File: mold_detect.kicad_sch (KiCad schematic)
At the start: 39 parts, among them J1 USB_C_Receptacle_USB2.0_14P, U1 SHT30-DIS, U2 TPL5010, U3 FT230XS, U4 W25Q128JVS, U5 ATmega328P-P, Y1 4MHz

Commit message: tpl5010 works!
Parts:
- added J2: ISP, Connector_IDC:IDC-Header_2x03_P2.54mm_Vertical, symbol Connector_Generic:Conn_02x03_Odd_Even
- added R11, R12: 100R, Resistor_SMD:R_0603_1608Metric_Pad0.98x0.95mm_HandSolder, symbol Device:R
- added Red2, Red3: LED, LED_THT:LED_D3.0mm, symbol Device:LED
- added SW2: usb_enable, symbol Switch:SW_DIP_x01
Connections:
- net +3V0: now also J2.2 (Pin_2)
- net CIPO: now also J2.1 (Pin_1)
- net COPI: now also J2.4 (Pin_4)
- net DONE: now also U5.6 (PD4); no longer U5.5 (PD3)
- net GND: now also R1.1, R2.1, J2.6 (Pin_6), R11.1, R12.1, SW2.1; no longer R1.2, R2.2, U3.13 (GND), U3.5 (GND)
- net HUM_LED: now also Blue1.2 (A); no longer Red1.2 (A)
- net RST: now also J2.5 (Pin_5)
- net SCK: now also J2.3 (Pin_3)
- net TEMP_LED: now also Red2.2 (A); no longer Blue1.2 (A)
- net WAKE_INTR: now also U5.5 (PD3); no longer U5.4 (PD2)
- net ERROR_LED: now reaches U5.13 (PD7)
- net ERROR_LED: now also Red1.2 (A)
- net USB_ENABLE_INTR: now reaches U5.23 (PC0)
- net USB_ENABLE_INTR: now also U3.13 (GND), U3.5 (GND), SW2.2
- net at Red1.1 (K): now also R11.2; no longer R1.1
- net at Blue1.1 (K): now also R2.2; no longer R2.1
- new net: R1.2, Red2.1 (K)
- new net: R12.2, Red3.1 (K)
- new net GENERAL_LED: Red3.2 (A), U5.4 (PD2)
- no-connect marks 18 -> 15
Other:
- note added: "ISP Port"
- note added: "The *two* 5k1 resistors at the C1 and C2 pins configure the USB C port for USB 2.0 operation. These aren't used when using a USB-A to USB-C cable. The USB Bus Powered Configuration is used (data sheet p. 18). The diode is needed to prevent the initial 3V3 laying on the USB-C port's VBUS when using a USB-C to USB-C cable. Without this the USB-C host won't enable USB 2.0 at 5V operation. The enable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"
- note added: "USB-C Port"
- note added: "Using 4MHz crystal and the internal 8div a clock speed of 0MHz5 is achieved. The internal crystal isn't accurate enough for UART. All unused pins will have an active internal pull up resistor and are configured as inputs to prevent a floating value. Using an external pull up could reduce power consumption. The internal pull-up on USB_ENABLE_INTR (PC0) is enabled. The one on WAKE_INTR (PD3) is dis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"
- note removed: "Port"
- note removed: "The *two* 5k1 resistors at the C1 and C2 pins configure the USB C port for USB 2.0 operation. These aren't used when using a USB-A to USB-C cable. The USB Bus Powered Configuration is used (data sheet p. 18). The diode is needed to prevent the initial 3V3 laying on the USB-C port's VBUS when using a USB-C to USB-C cable. Without this the USB-C host won't enable USB 2.0 at 5V operation."
- note removed: "Using 4MHz crystal and the internal 8div a clock speed of 0MHz5 is achieved. The internal crystal isn't accurate enough for UART. All unused pins will have an active internal pull up resistor and are configured as inputs to prevent a floating value. Using an external pull up could reduce power consumption."
- note removed: "high hum"
- note removed: "low temp"
- moved on the sheet: BT1, Blue1, C1, C10, C11, C2, C3, C4, C5, C6, C7, C8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

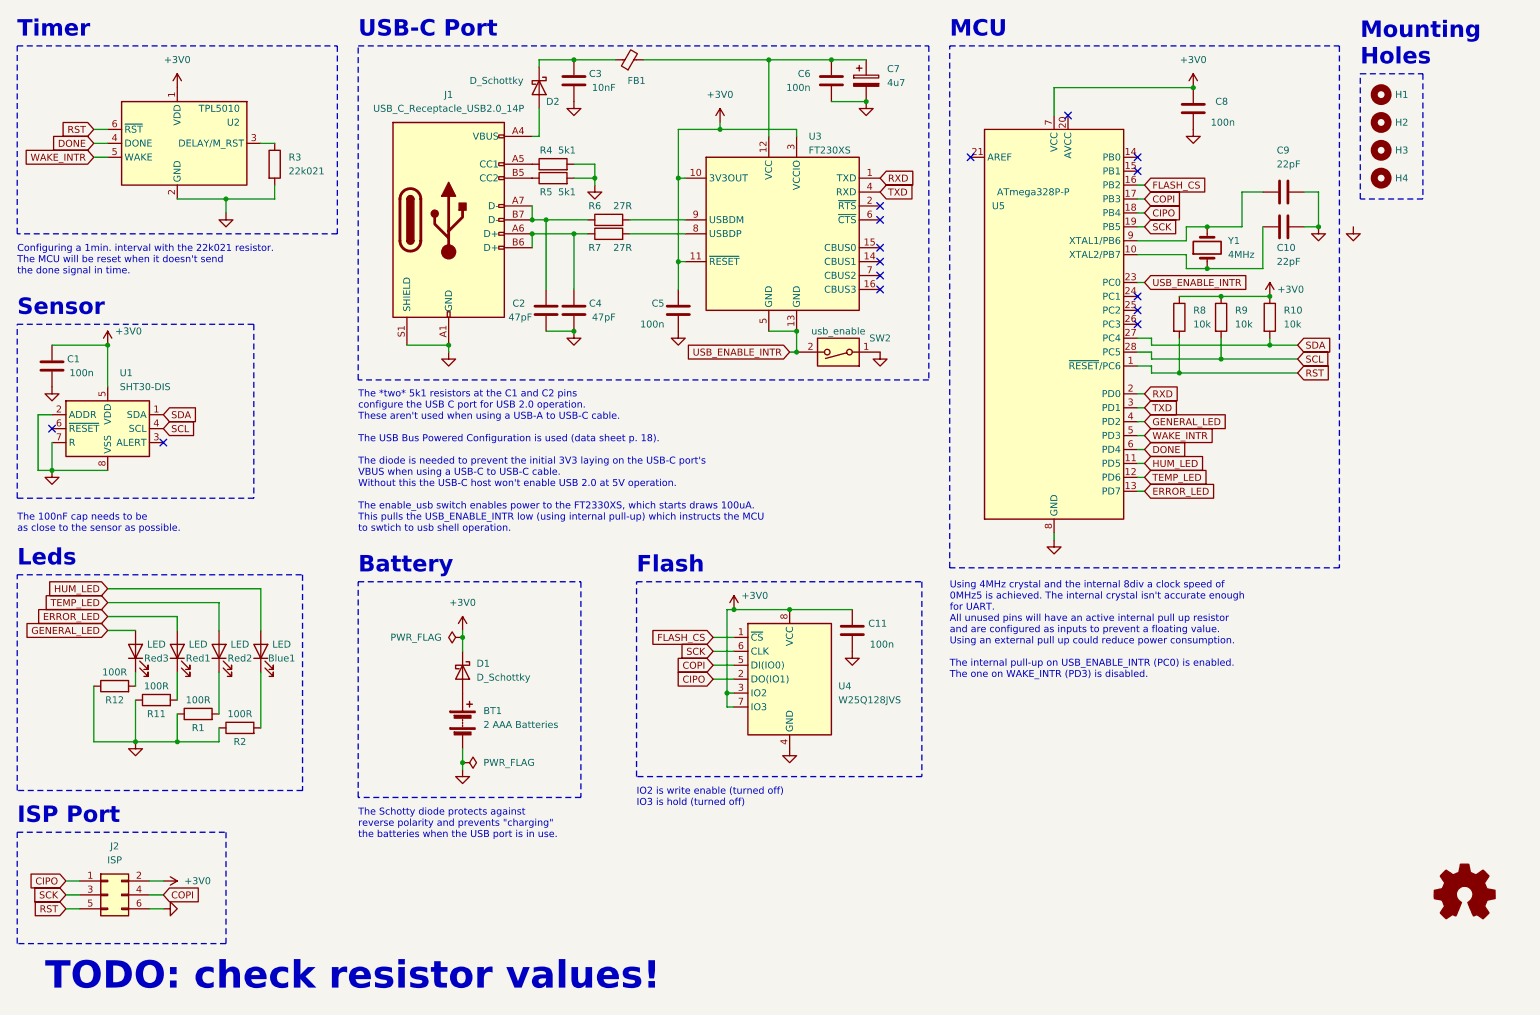
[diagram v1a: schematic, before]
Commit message: updated footprints; started layout
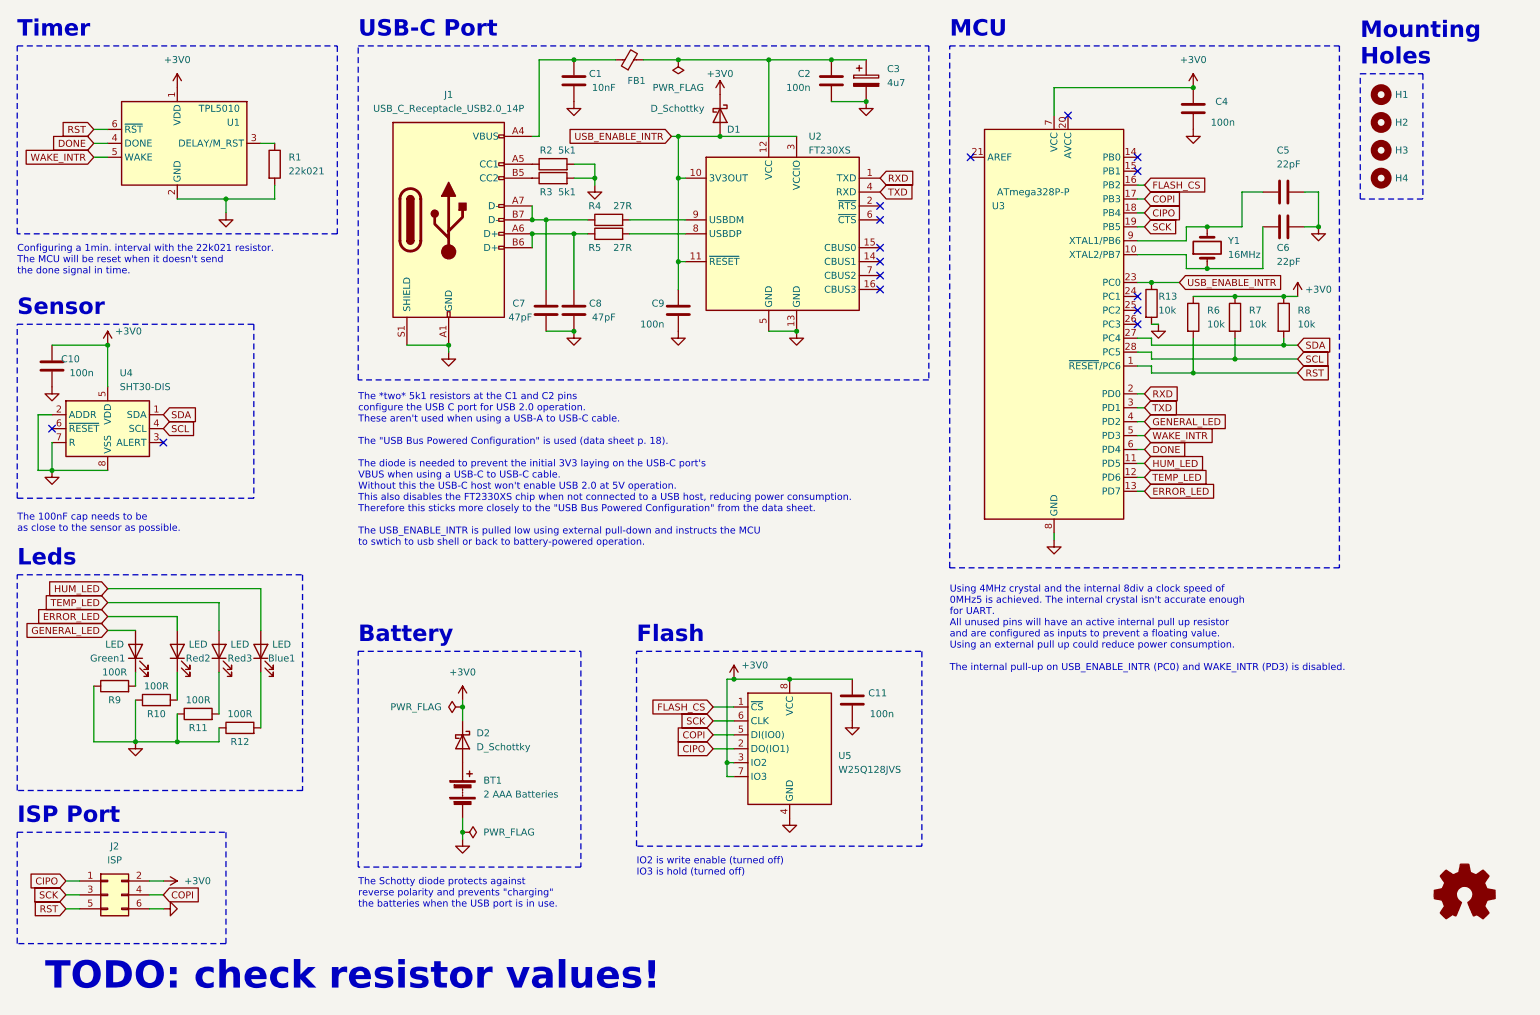
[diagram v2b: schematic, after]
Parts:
- removed D2: D_Schottky, Diode_SMD:D_SOD-323_HandSoldering, symbol Device:D_Schottky
- removed SW2: usb_enable, symbol Switch:SW_DIP_x01
- added D1: D_Schottky, Diode_SMD:D_SOD-323_HandSoldering, symbol Device:D_Schottky
- added R13: 10k, Resistor_SMD:R_0603_1608Metric_Pad0.98x0.95mm_HandSolder, symbol Device:R
- C3: renamed from C7; footprint (none) -> Capacitor_THT:CP_Radial_D5.0mm_P2.00mm
- FB1: footprint (none) -> Capacitor_SMD:C_0603_1608Metric_Pad1.08x0.95mm_HandSolder
- Y1: value 4MHz -> 16MHz; footprint (none) -> Crystal:Crystal_HC49-4H_Vertical
- renumbered C3 to C1, C1 to C10, C6 to C2, C8 to C4, C9 to C5, C10 to C6, C2 to C7, C4 to C8, C5 to C9, D1 to D2, Red3 to Green1, R3 to R1, R11 to R10, R1 to R11, R2 to R12, R4 to R2, R5 to R3, R6 to R4, R7 to R5, R8 to R6, R9 to R7, R10 to R8, R12 to R9, Red1 to Red2, Red2 to Red3, U2 to U1, U3 to U2, U5 to U3, U1 to U4, U4 to U5
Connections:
- net +3V0: now also D1.1 (K); no longer C9.2, U2.10 (3V3OUT), U2.11 (~{RESET}), U2.3 (VCCIO)
- net GND: now also U2.13 (GND), U2.5 (GND), R13.2
- net USB_ENABLE_INTR: now also C9.2, U2.10 (3V3OUT), U2.11 (~{RESET}), U2.3 (VCCIO), D1.2 (A), R13.1; no longer U2.13 (GND), U2.5 (GND)
- net at J1.A4 (VBUS), J1.A9 (VBUS), J1.B4 (VBUS)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: now also C1.2, FB1.1
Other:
- note added: "The *two* 5k1 resistors at the C1 and C2 pins configure the USB C port for USB 2.0 operation. These aren't used when using a USB-A to USB-C cable. The "USB Bus Powered Configuration" is used (data sheet p. 18). The diode is needed to prevent the initial 3V3 laying on the USB-C port's VBUS when using a USB-C to USB-C cable. Without this the USB-C host won't enable USB 2.0 at 5V operation. This als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"
- note added: "Using 4MHz crystal and the internal 8div a clock speed of 0MHz5 is achieved. The internal crystal isn't accurate enough for UART. All unused pins will have an active internal pull up resistor and are configured as inputs to prevent a floating value. Using an external pull up could reduce power consumption. The internal pull-up on USB_ENABLE_INTR (PC0) and WAKE_INTR (PD3) is disabled."
- note removed: "The *two* 5k1 resistors at the C1 and C2 pins configure the USB C port for USB 2.0 operation. These aren't used when using a USB-A to USB-C cable. The USB Bus Powered Configuration is used (data sheet p. 18). The diode is needed to prevent the initial 3V3 laying on the USB-C port's VBUS when using a USB-C to USB-C cable. Without this the USB-C host won't enable USB 2.0 at 5V operation. The enable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"
- note removed: "Using 4MHz crystal and the internal 8div a clock speed of 0MHz5 is achieved. The internal crystal isn't accurate enough for UART. All unused pins will have an active internal pull up resistor and are configured as inputs to prevent a floating value. Using an external pull up could reduce power consumption. The internal pull-up on USB_ENABLE_INTR (PC0) is enabled. The one on WAKE_INTR (PD3) is dis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"
- moved on the sheet: BT1, C11, D2, R6, R7, R8, U5

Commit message: updated PCB design
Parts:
- added C4: 100n, Capacitor_SMD:C_0603_1608Metric_Pad1.08x0.95mm_HandSolder, symbol Device:C
- renumbered C9 to C10, C10 to C11, C11 to C12, C4 to C5, C5 to C6, C6 to C7, C7 to C8, C8 to C9, R9 to R10, R10 to R11, R11 to R12, R12 to R13, R13 to R6, R6 to R7, R7 to R8, R8 to R9, Red2 to Red1, Red3 to Red2
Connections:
- net +3V0: now also C4.2
- net GENERAL_LED: now also U3.11 (PD5); no longer U3.4 (PD2)
- net GND: now also C4.1
- net HUM_LED: now also U3.12 (PD6); no longer U3.11 (PD5)
- net TEMP_LED: now also U3.4 (PD2); no longer U3.12 (PD6)

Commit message: added blender
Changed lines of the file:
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@@
 		(at 278.13 173.99 0)
 		(unit 1)
-		(exclude_from_sim no)
+		(exclude_from_sim yes)
 		(in_bom no)
 		(on_board no)
@@
 		)
 		(property "Description" "Open Hardware logo, small"
-			(at 278.13 173.99 0)
-			(effects
-				(font
-					(size 1.27 1.27)
-				)
-				(hide yes)
-			)
-		)
-		(property "Sim.Enable" "0"
 			(at 278.13 173.99 0)
 			(effects
@@
 		(dnp no)
 		(property "Reference" "C11"
-			(at 25.4 76.2 0)
-			(effects
-				(font
+			(at 26.67 76.2 0)
+			(effects
+				(font

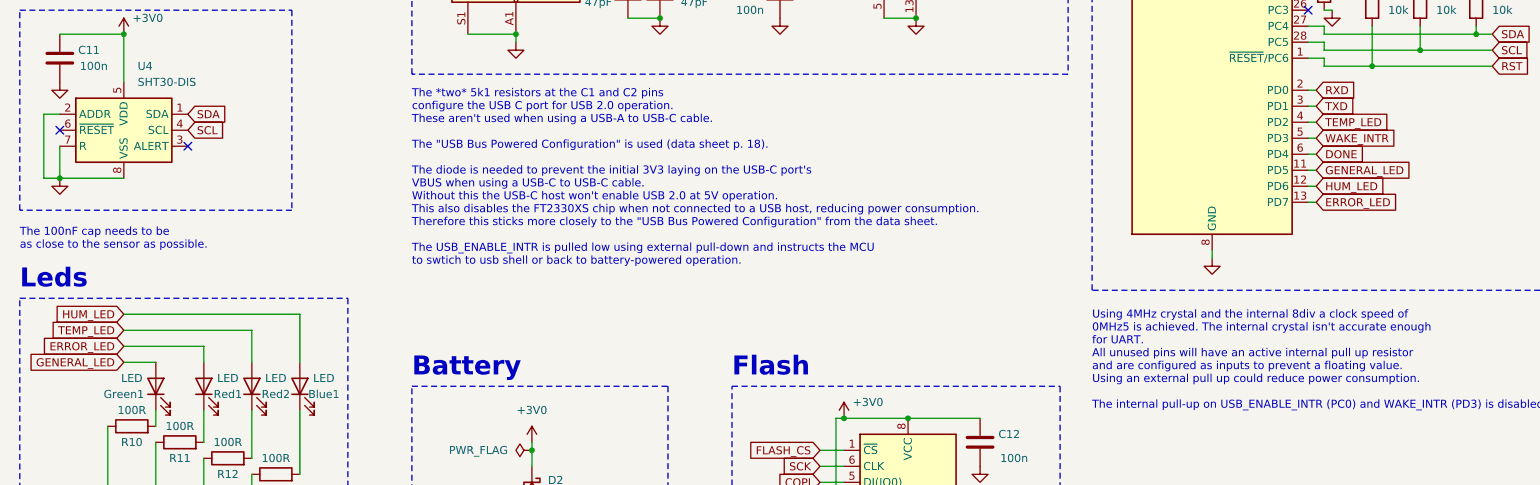
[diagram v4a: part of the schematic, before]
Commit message: feat: implemented flash power down
closes #1
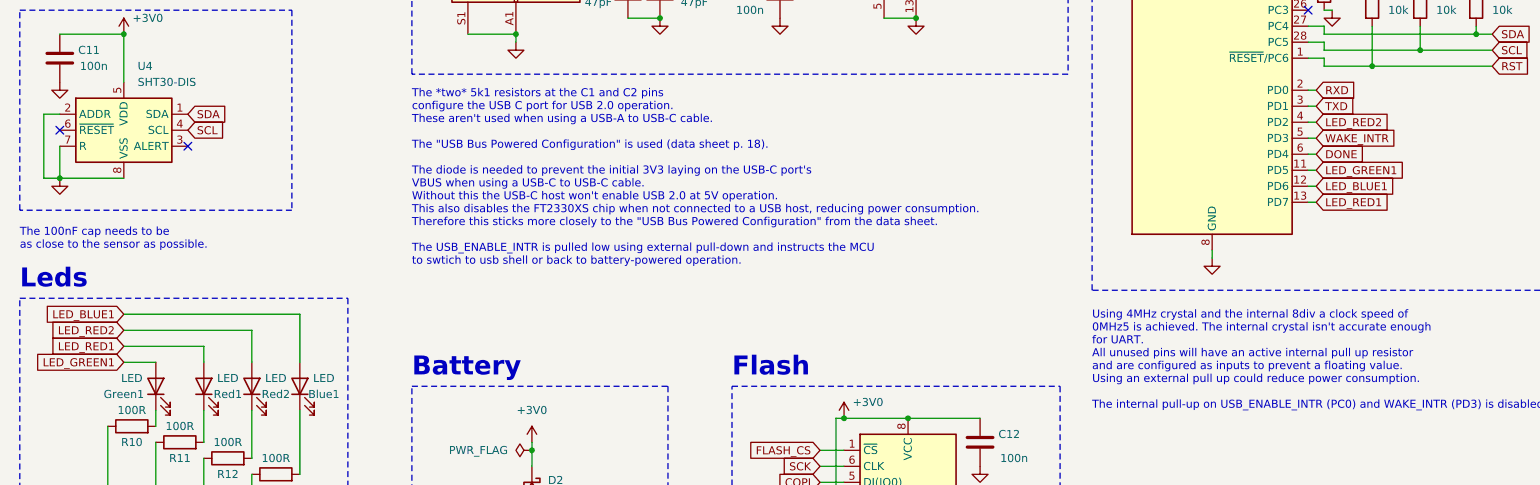
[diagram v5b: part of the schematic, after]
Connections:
- net ERROR_LED renamed LED_RED1
- net GENERAL_LED renamed LED_GREEN1
- net HUM_LED renamed LED_BLUE1
- net TEMP_LED renamed LED_RED2
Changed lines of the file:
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@@
 		)
 	)
-	(global_label "HUM_LED"
+	(global_label "LED_BLUE1"
 		(shape input)
 		(at 30.48 118.11 180)
@@
 		)
 	)
-	(global_label "TEMP_LED"
+	(global_label "LED_RED2"
 		(shape input)
 		(at 30.48 120.65 180)
@@
 		)
 	)
-	(global_label "ERROR_LED"
+	(global_label "LED_RED1"
 		(shape input)
 		(at 219.71 100.33 0)
@@
 		)
 	)
-	(global_label "GENERAL_LED"
+	(global_label "LED_GREEN1"
 		(shape input)
 		(at 30.48 125.73 180)
@@
 		)
 	)
-	(global_label "GENERAL_LED"
+	(global_label "LED_GREEN1"
 		(shape input)
 		(at 219.71 95.25 0)
@@
 		)
 	)
-	(global_label "ERROR_LED"
+	(global_label "LED_RED1"
 		(shape input)
 		(at 30.48 123.19 180)
@@
 		)
 	)
-	(global_label "HUM_LED"
+	(global_label "LED_BLUE1"
 		(shape input)
 		(at 219.71 97.79 0)
@@
 		)
 	)
-	(global_label "TEMP_LED"
+	(global_label "LED_RED2"
 		(shape input)
 		(at 219.71 87.63 0)
